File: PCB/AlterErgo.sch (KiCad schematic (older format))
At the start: 94 parts, among them J1 GS3, J2 SJ-43514, J3 GS3, SW0:10 SW_Push, SW0:11 SW_Push, SW0:12 SW_Push, SW0:7 SW_Push, SW0:8 SW_Push, SW0:9 SW_Push, SW1 SW_SPST, SW1:10 SW_Push, SW1:11 SW_Push, SW1:12 SW_Push, SW1:13 SW_Push, SW1:7 SW_Push, SW1:8 SW_Push, SW1:9 SW_Push, SW2:10 SW_Push, SW2:11 SW_Push, SW2:12 SW_Push, SW2:13 SW_Push, SW2:7 SW_Push, SW2:8 SW_Push, SW2:9 SW_Push, SW3:10 SW_Push, SW3:11 SW_Push, SW3:12 SW_Push, SW3:13 SW_Push, SW3:8 SW_Push, SW3:9 SW_Push, SW4:10 SW_Push, SW4:11 SW_Push, SW4:12 SW_Push, SW4:13 SW_Push, SW4:7 SW_Push, SW4:8 SW_Push, SW4:9 SW_Push, SW5:10 SW_Push, SW5:11 SW_Push, SW5:12 SW_Push, SW5:13 SW_Push, SW5:7 SW_Push, SW5:8 SW_Push, SW5:9 SW_Push, U1 Feather32u4Bluefruit, U2 MCP23018

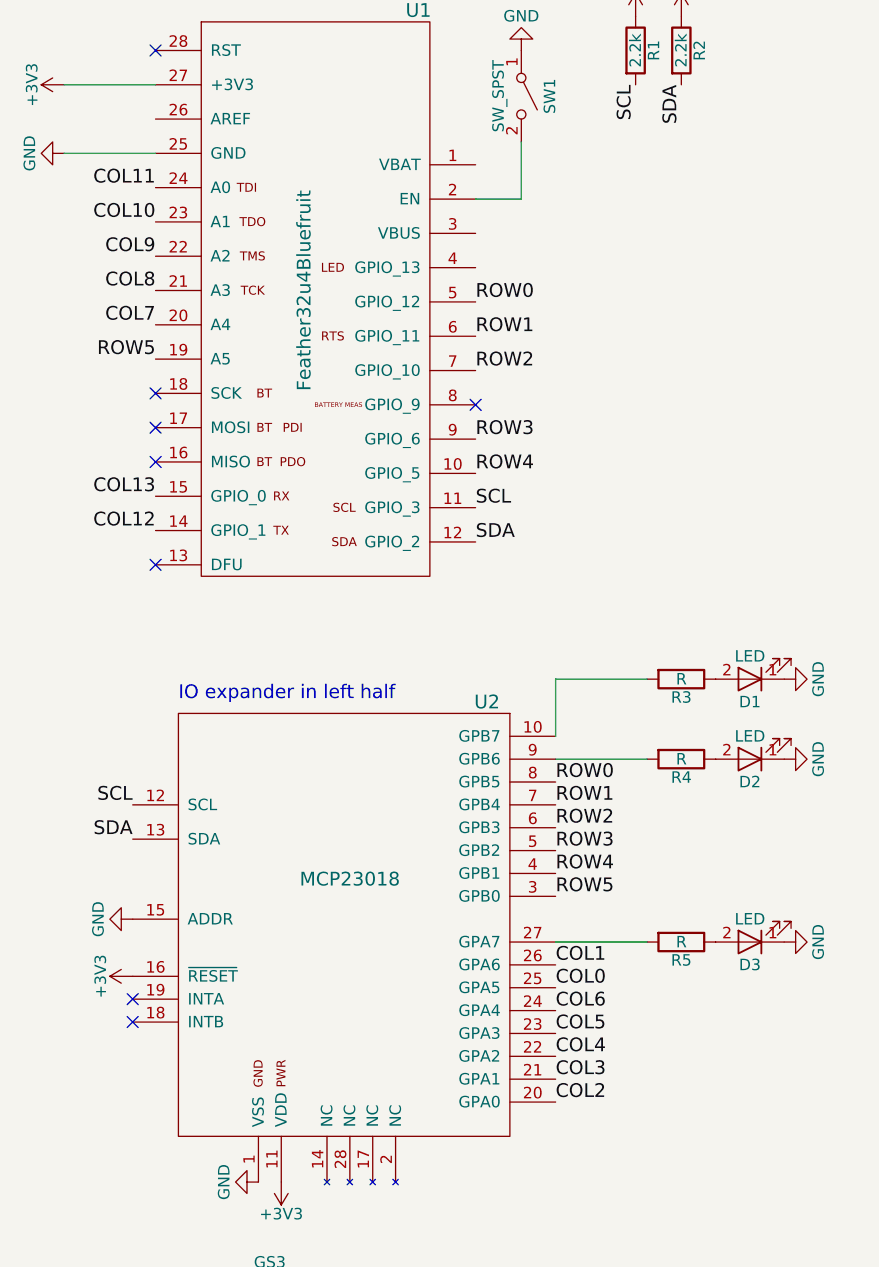
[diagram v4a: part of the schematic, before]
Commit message: Rework row/col pin assignments on Feather to line up better with those on the i/o expander
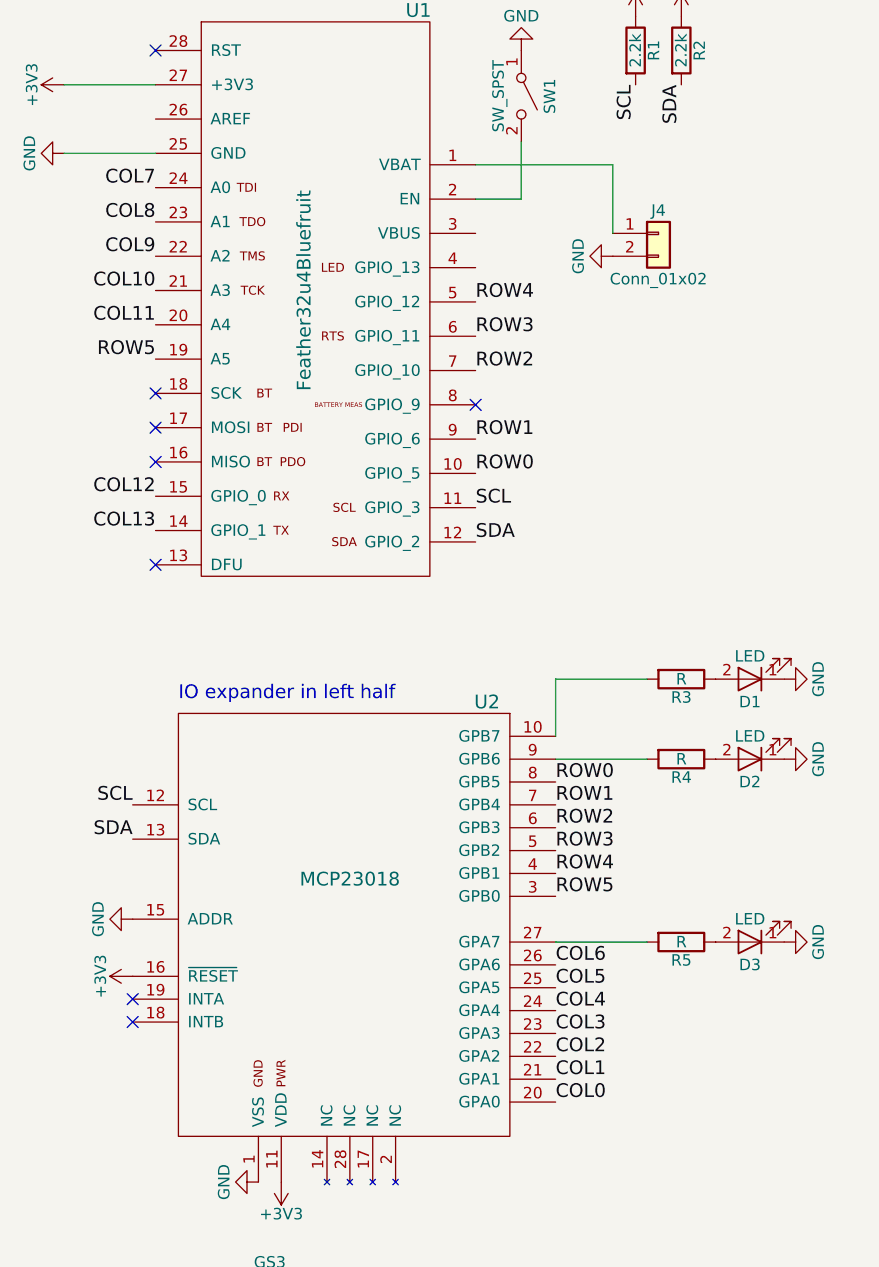
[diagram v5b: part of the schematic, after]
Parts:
- added J4: Conn_01x02, Connectors_JST:JST_PH_S2B-PH-SM4-TB_02x2.00mm_Angled, symbol Conn_01x02
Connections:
- net COL0: now also U1.14 (GPIO_1), U2.20 (GPA0); no longer U1.15 (GPIO_0), U2.25 (GPA5)
- net COL1: now also U1.15 (GPIO_0), U2.21 (GPA1); no longer U1.14 (GPIO_1), U2.26 (GPA6)
- net COL10: now also U1.21 (A3), U2.23 (GPA3); no longer U1.23 (A1), U2.21 (GPA1)
- net COL11: now also U1.20 (A4), U2.22 (GPA2); no longer U1.24 (A0), U2.20 (GPA0)
- net COL4: now also U2.24 (GPA4); no longer U2.22 (GPA2)
- net COL5: now also U1.23 (A1), U2.25 (GPA5); no longer U1.21 (A3), U2.23 (GPA3)
- net COL6: now also U1.24 (A0), U2.26 (GPA6); no longer U1.20 (A4), U2.24 (GPA4)
- net GND: now also J4.2 (Pin_2)
- net ROW0: now also U1.10 (GPIO_5); no longer U1.5 (GPIO_12)
- net ROW1: now also U1.9 (GPIO_6); no longer U1.6 (GPIO_11)
- net ROW3: now also U1.6 (GPIO_11); no longer U1.9 (GPIO_6)
- net ROW4: now also U1.5 (GPIO_12); no longer U1.10 (GPIO_5)
- net at U1.1 (VBAT): now also J4.1 (Pin_1)
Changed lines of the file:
@@
 Text Label 10000 6000 0    60   ~ 0
 COL13
-Text Label 2850 2000 0    60   ~ 0
+Text Label 2850 2750 0    60   ~ 0
 ROW0
-Text Label 2850 2150 0    60   ~ 0
+Text Label 2850 2600 0    60   ~ 0
 ROW1
 Text Label 2850 2300 0    60   ~ 0
 ROW2
-Text Label 2850 2600 0    60   ~ 0
+Text Label 2850 2150 0    60   ~ 0
 ROW3
-Text Label 2850 2750 0    60   ~ 0
+Text Label 2850 2000 0    60   ~ 0
 ROW4
 Text Label 1450 2250 2    60   ~ 0
 ROW5
-Text Label 1450 2100 2    60   ~ 0
+Text Label 1450 1500 2    60   ~ 0
 COL7
-Text Label 1450 1950 2    60   ~ 0
+Text Label 1450 1650 2    60   ~ 0
 COL8
 Text Label 1450 1800 2    60   ~ 0
 COL9
-Text Label 1450 1650 2    60   ~ 0
+Text Label 1450 1950 2    60   ~ 0
 COL10
-Text Label 1450 1500 2    60   ~ 0
+Text Label 1450 2100 2    60   ~ 0
 COL11
+Text Label 1450 2850 2    60   ~ 0
+COL12
 Text Label 1450 3000 2    60   ~ 0
-COL12
-Text Label 1450 2850 2    60   ~ 0
 COL13
+Text Label 3200 5500 0    60   ~ 0
+COL0
+Text Label 3200 5400 0    60   ~ 0
+COL1
+Text Label 3200 5300 0    60   ~ 0
+COL2
+Text Label 3200 5200 0    60   ~ 0
+COL3
+Text Label 3200 5100 0    60   ~ 0
+COL4
 Text Label 3200 5000 0    60   ~ 0
-COL0
+COL5
 Text Label 3200 4900 0    60   ~ 0
-COL1
-Text Label 3200 5500 0    60   ~ 0
-COL2
-Text Label 3200 5400 0    60   ~ 0
-COL3
-Text Label 3200 5300 0    60   ~ 0
-COL4
-Text Label 3200 5200 0    60   ~ 0
-COL5
-Text Label 3200 5100 0    60   ~ 0
 COL6
 Text Label 3200 4100 0    60   ~ 0
@@
 	0    -1   -1   0
 $EndComp
+$Comp
+L Conn_01x02 J4
+U 1 1 5B21D76B
+P 3650 1700
+F 0 "J4" H 3650 1800 50  0000 C CNN
+F 1 "Conn_01x02" H 3650 1500 50  0000 C CNN
+F 2 "Connectors_JST:JST_PH_S2B-PH-SM4-TB_02x2.00mm_Angled" H 3650 1700 50  0001 C CNN
+F 3 "" H 3650 1700 50  0001 C CNN
+	1    3650 1700
+	1    0    0    -1
+$EndComp
+$Comp
+L GND #PWR017
+U 1 1 5B21E9A5
+P 3450 1800
+F 0 "#PWR017" H 3450 1550 50  0001 C CNN
+F 1 "GND" H 3450 1650 50  0000 C CNN
+F 2 "" H 3450 1800 50  0001 C CNN
+F 3 "" H 3450 1800 50  0001 C CNN
+	1    3450 1800
+	0    1    1    0
+$EndComp
+Wire Wire Line
+	2850 1400 3450 1400
+Wire Wire Line
+	3450 1400 3450 1700
 $EndSCHEMATC

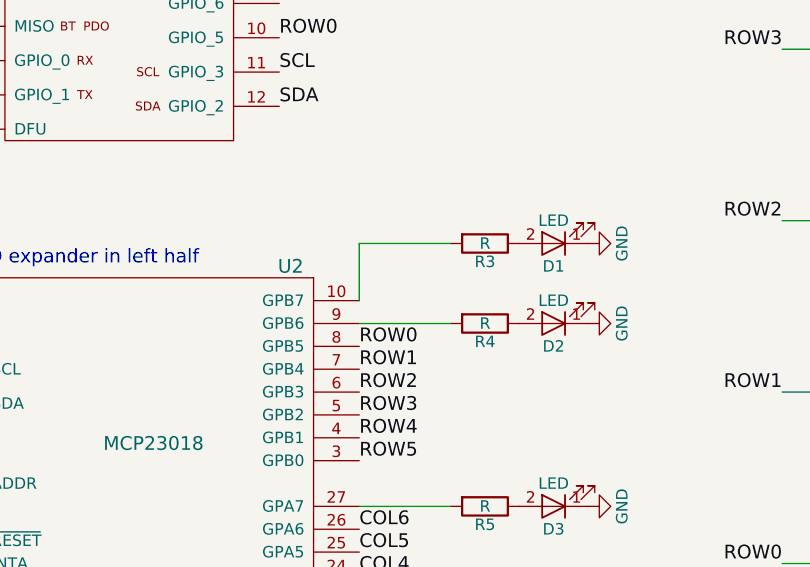
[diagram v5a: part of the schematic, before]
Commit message: Initial attempt at routing traces in upper area
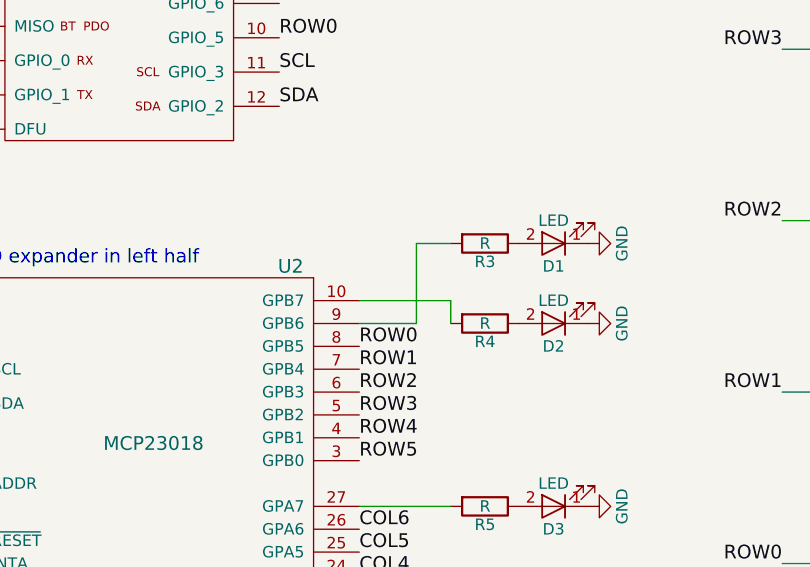
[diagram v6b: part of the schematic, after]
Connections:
- net at U2.10 (GPB7): now also R4.2; no longer R3.2
- net at U2.9 (GPB6): now also R3.2; no longer R4.2
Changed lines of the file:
@@
 $EndComp
-Wire Wire Line
-	3600 3650 3200 3650
-Wire Wire Line
-	3200 3650 3200 3900
-Wire Wire Line
-	3200 4000 3600 4000
 Wire Wire Line
 	3600 4800 3200 4800
@@
 Wire Wire Line
 	3450 1400 3450 1700
+Wire Wire Line
+	3200 3900 3600 3900
+Wire Wire Line
+	3600 3900 3600 4000
+Wire Wire Line
+	3200 4000 3450 4000
+Wire Wire Line
+	3450 4000 3450 3650
+Wire Wire Line
+	3450 3650 3600 3650
 $EndSCHEMATC

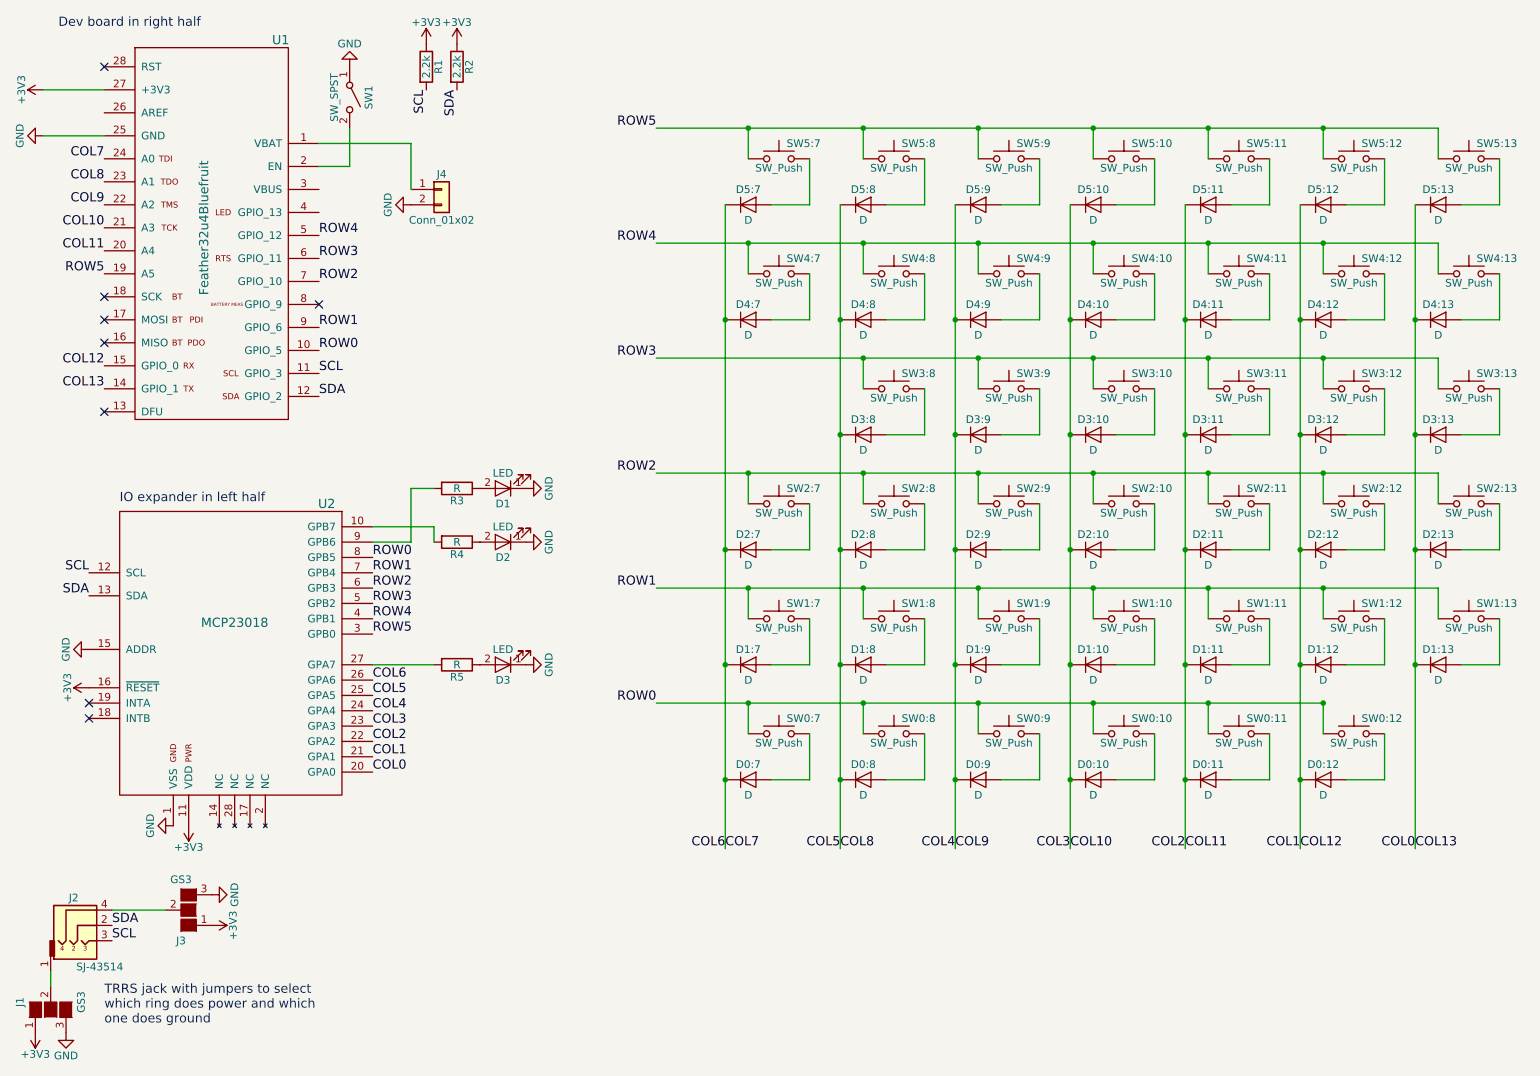
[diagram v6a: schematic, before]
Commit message: Remove separate battery connector points; position Feather underneath the PCB
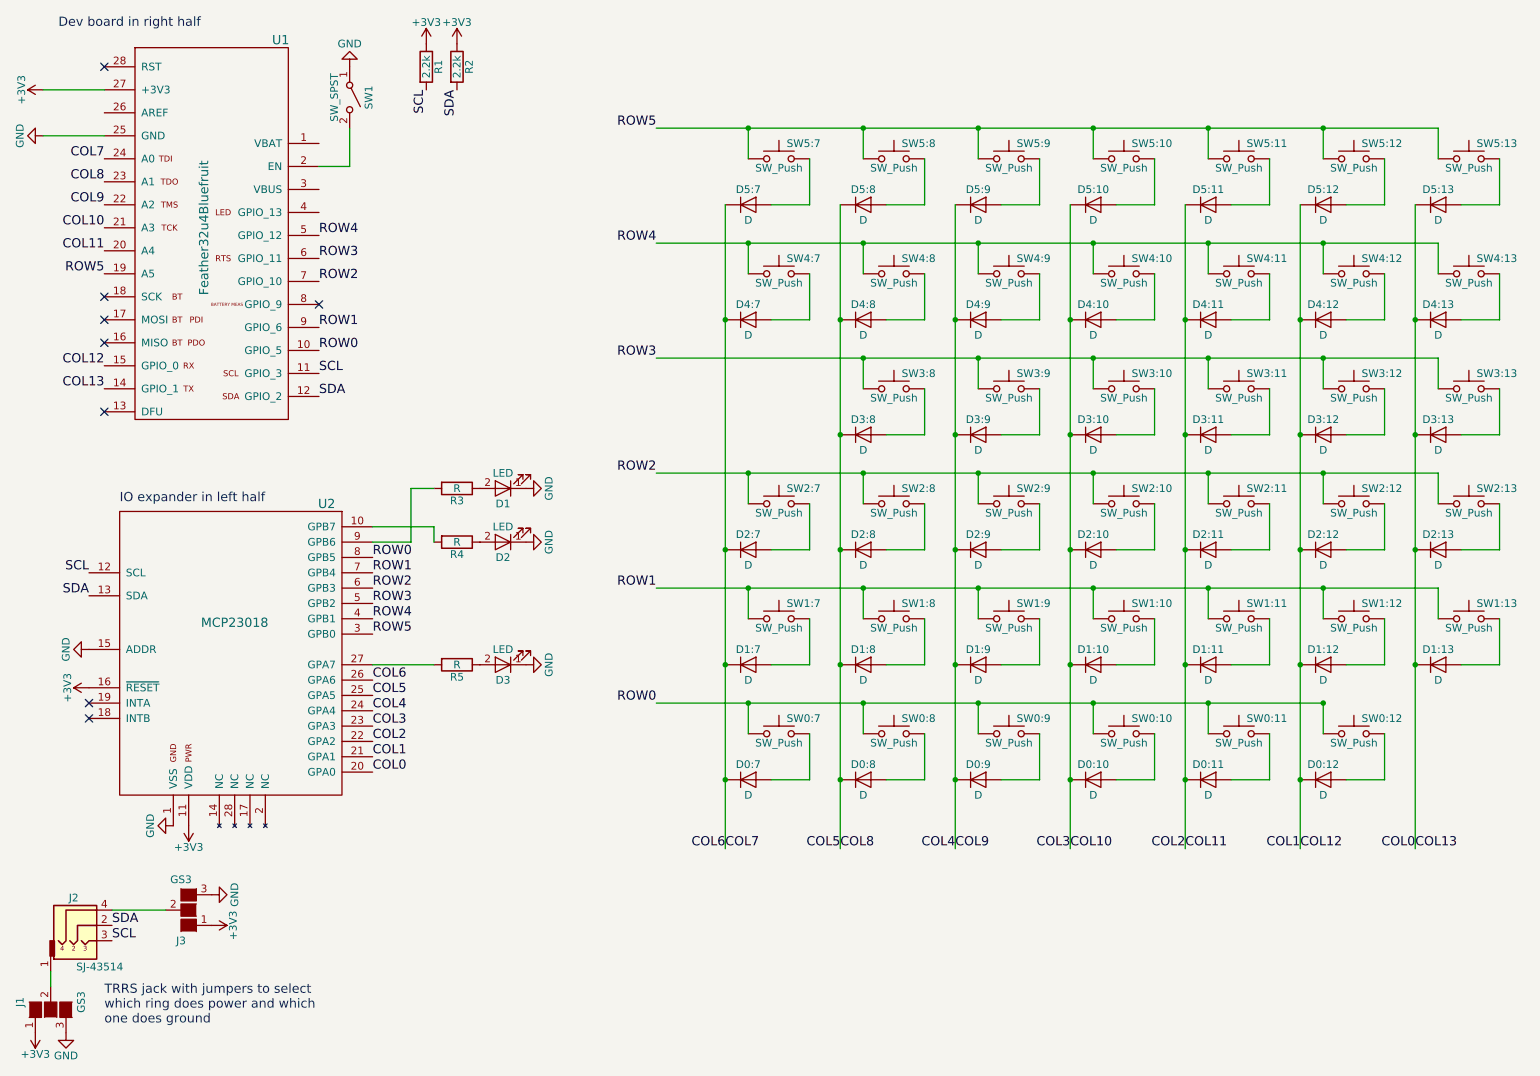
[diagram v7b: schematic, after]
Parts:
- removed J4: Conn_01x02, Connectors_JST:JST_PH_S2B-PH-SM4-TB_02x2.00mm_Angled, symbol Conn_01x02
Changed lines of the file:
@@
 	9800 5550 9550 5550
 Wire Wire Line
-	5050 1300 10150 1300
-Wire Wire Line
-	5050 2050 10150 2050
-Wire Wire Line
-	5050 2800 10150 2800
-Wire Wire Line
-	5050 3550 10150 3550
-Wire Wire Line
-	5050 4300 10150 4300
-Wire Wire Line
-	5050 5050 9400 5050
-Wire Wire Line
-	5500 1800 5500 6000
-Wire Wire Line
-	6250 1800 6250 6000
-Wire Wire Line
-	7000 1800 7000 6000
-Wire Wire Line
-	7750 1800 7750 6000
-Wire Wire Line
-	8500 1800 8500 6000
-Wire Wire Line
-	9250 1800 9250 6000
-Wire Wire Line
-	10000 1800 10000 6000
+	5050 1300 5650 1300
+Wire Wire Line
+	5650 1300 6400 1300
+Wire Wire Line
+	6400 1300 7150 1300
+Wire Wire Line
+	7150 1300 7900 1300
+Wire Wire Line
+	7900 1300 8650 1300
+Wire Wire Line
+	8650 1300 9400 1300
+Wire Wire Line
+	9400 1300 10150 1300
+Wire Wire Line
+	5050 2050 5650 2050
+Wire Wire Line
+	5650 2050 6400 2050
+Wire Wire Line
+	6400 2050 7150 2050
+Wire Wire Line
+	7150 2050 7900 2050
+Wire Wire Line
+	7900 2050 8650 2050
+Wire Wire Line
+	8650 2050 9400 2050
+Wire Wire Line
+	9400 2050 10150 2050
+Wire Wire Line
+	5050 2800 6400 2800
+Wire Wire Line
+	6400 2800 7150 2800
+Wire Wire Line
+	7150 2800 7900 2800
+Wire Wire Line
+	7900 2800 8650 2800
+Wire Wire Line
+	8650 2800 9400 2800
+Wire Wire Line
+	9400 2800 10150 2800
+Wire Wire Line
+	5050 3550 5650 3550
+Wire Wire Line
+	5650 3550 6400 3550
+Wire Wire Line
+	6400 3550 7150 3550
+Wire Wire Line
+	7150 3550 7900 3550
+Wire Wire Line
+	7900 3550 8650 3550
+Wire Wire Line
+	8650 3550 9400 3550
+Wire Wire Line
+	9400 3550 10150 3550
+Wire Wire Line
+	5050 4300 5650 4300
+Wire Wire Line
+	5650 4300 6400 4300
+Wire Wire Line
+	6400 4300 7150 4300
+Wire Wire Line
+	7150 4300 7900 4300
+Wire Wire Line
+	7900 4300 8650 4300
+Wire Wire Line
+	8650 4300 9400 4300
+Wire Wire Line
+	9400 4300 10150 4300
+Wire Wire Line
+	5050 5050 5650 5050
+Wire Wire Line
+	5650 5050 6400 5050
+Wire Wire Line
+	6400 5050 7150 5050
+Wire Wire Line
+	7150 5050 7900 5050
+Wire Wire Line
+	7900 5050 8650 5050
+Wire Wire Line
+	8650 5050 9400 5050
+Wire Wire Line
+	5500 1800 5500 2550
+Wire Wire Line
+	5500 2550 5500 4050
+Wire Wire Line
+	5500 4050 5500 4800
+Wire Wire Line
+	5500 4800 5500 5550
+Wire Wire Line
+	5500 5550 5500 6000
+Wire Wire Line
+	6250 1800 6250 2550
+Wire Wire Line
+	6250 2550 6250 3300
+Wire Wire Line
+	6250 3300 6250 4050
+Wire Wire Line
+	6250 4050 6250 4800
+Wire Wire Line
+	6250 4800 6250 5550
+Wire Wire Line
+	6250 5550 6250 6000
+Wire Wire Line
+	7000 1800 7000 2550
+Wire Wire Line
+	7000 2550 7000 3300
+Wire Wire Line
+	7000 3300 7000 4050
+Wire Wire Line
+	7000 4050 7000 4800
+Wire Wire Line
+	7000 4800 7000 5550
+Wire Wire Line
+	7000 5550 7000 6000
+Wire Wire Line
+	7750 1800 7750 2550
+Wire Wire Line
+	7750 2550 7750 3300
+Wire Wire Line
+	7750 3300 7750 4050
+Wire Wire Line
+	7750 4050 7750 4800
+Wire Wire Line
+	7750 4800 7750 5550
+Wire Wire Line
+	7750 5550 7750 6000
+Wire Wire Line
+	8500 1800 8500 2550
+Wire Wire Line
+	8500 2550 8500 3300
+Wire Wire Line
+	8500 3300 8500 4050
+Wire Wire Line
+	8500 4050 8500 4800
+Wire Wire Line
+	8500 4800 8500 5550
+Wire Wire Line
+	8500 5550 8500 6000
+Wire Wire Line
+	9250 1800 9250 2550
+Wire Wire Line
+	9250 2550 9250 3300
+Wire Wire Line
+	9250 3300 9250 4050
+Wire Wire Line
+	9250 4050 9250 4800
+Wire Wire Line
+	9250 4800 9250 5550
+Wire Wire Line
+	9250 5550 9250 6000
+Wire Wire Line
+	10000 1800 10000 2550
+Wire Wire Line
+	10000 2550 10000 3300
+Wire Wire Line
+	10000 3300 10000 4050
+Wire Wire Line
+	10000 4050 10000 4800
+Wire Wire Line
+	10000 4800 10000 6000
 Connection ~ 5650 1300
 Connection ~ 6400 1300
@@
 	0    -1   -1   0
 $EndComp
-$Comp
-L Conn_01x02 J4
-U 1 1 5B21D76B
-P 3650 1700
-F 0 "J4" H 3650 1800 50  0000 C CNN
-F 1 "Conn_01x02" H 3650 1500 50  0000 C CNN
-F 2 "Connectors_JST:JST_PH_S2B-PH-SM4-TB_02x2.00mm_Angled" H 3650 1700 50  0001 C CNN
-F 3 "" H 3650 1700 50  0001 C CNN
-	1    3650 1700
-	1    0    0    -1
-$EndComp
-$Comp
-L GND #PWR017
-U 1 1 5B21E9A5
-P 3450 1800
-F 0 "#PWR017" H 3450 1550 50  0001 C CNN
-F 1 "GND" H 3450 1650 50  0000 C CNN
-F 2 "" H 3450 1800 50  0001 C CNN
-F 3 "" H 3450 1800 50  0001 C CNN
-	1    3450 1800
-	0    1    1    0
-$EndComp
-Wire Wire Line
-	2850 1400 3450 1400
-Wire Wire Line
-	3450 1400 3450 1700
 Wire Wire Line
 	3200 3900 3600 3900
